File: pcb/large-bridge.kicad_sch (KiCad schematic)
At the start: 8 parts, among them Q21 GANE3R9, Q22 GANE3R9, U10 LMG1205

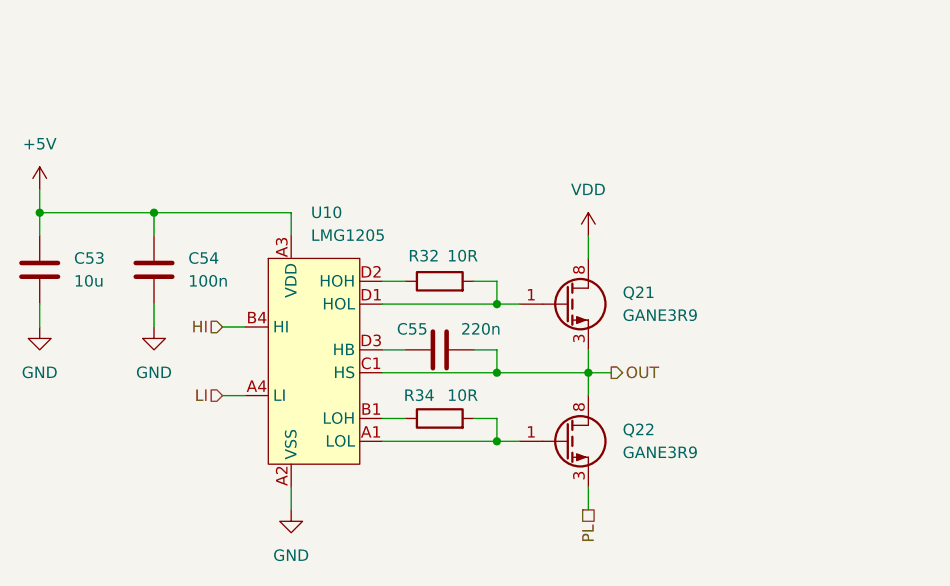
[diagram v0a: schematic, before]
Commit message: Finish rough layout
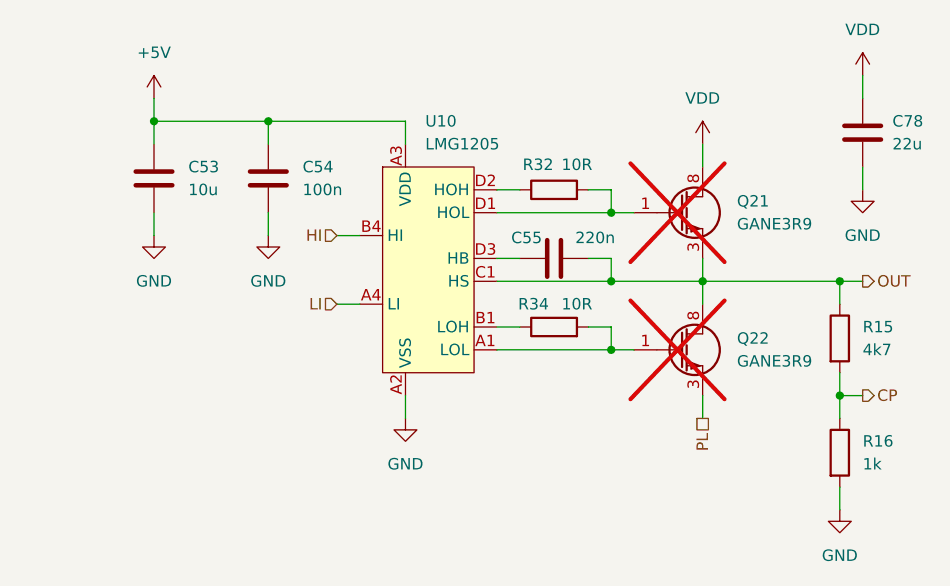
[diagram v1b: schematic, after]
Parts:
- added C78: 22u, Capacitor_SMD:C_0805_2012Metric, symbol Device:C
- added R15: 4k7, Resistor_SMD:R_0402_1005Metric, symbol Device:R
- added R16: 1k, Resistor_SMD:R_0402_1005Metric, symbol Device:R
- Q21, Q22: now not fitted
- R32, R34: LCSC C25139 -> C25077
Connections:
- net GND: now also C78.2, R16.2
- net OUT: now also R15.1
- net VDD: now also C78.1
- new net CP: R15.2, R16.1
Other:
- moved on the sheet: C53, C54, C55, R32, R34, U10

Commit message: Save old buck regulator
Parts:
- removed C78: 22u, Capacitor_SMD:C_0805_2012Metric, symbol Device:C
- R15: value 4k7 -> 10k; LCSC C25900 -> C25744
- R16: value 1k -> 1k5; LCSC C11702 -> C25867
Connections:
- net CP: now also R15.1; no longer R15.2
- net OUT: now also R15.2; no longer R15.1
